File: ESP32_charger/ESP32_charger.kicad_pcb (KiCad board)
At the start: 2 copper layers, 58.2 x 36.8 mm, 60 parts, among them J1 USB_C_Receptacle_USB2.0_16P, J2 Conn_01x04_Pin, Q2 BC817W, Q3 HL-2301V, SW1 SW_Push, SW2 SW_Push, U1 ESP32-WROOM-32, U2 XM5062S, U3 HT2348ARTZ8, U4 INA219AxDCN

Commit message: update to order version
placed silkscreen
placed logos
add 3d models
generate 3d model
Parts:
- added G***: LOGO, TheBrutzlers_Lib:thebrutzler_10mm_mod, F.Cu at (96.8, 68.2)
- added REF**: OSHW-Logo2_9.8x8mm_SilkScreen, Symbol:OSHW-Logo2_9.8x8mm_SilkScreen, F.Cu at (96.2, 88.5)
- added REF**: KiCad-Logo2_6mm_SilkScreen, Symbol:KiCad-Logo2_6mm_SilkScreen, F.Cu at (84.0, 87.5)
- added SM3: SYM_Arrow45_Tiny, TheBrutzlers_Lib:Symbol_kurzschlussblog, F.Cu at (102.2, 70.9)
- SW1, SW2: footprint TheBrutzlers_Lib:microswitch -> Button_Switch_SMD:SW_SPST_CK_RS282G05A3
- moved SW2 5.34 mm to (105.5, 90.2)
- moved SW1 2.67 mm to (126.8, 90.2)
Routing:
- net Net-(U1-IO48): track 39.4 -> 45.5 mm
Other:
- board text added: "+"
- board text added: "-"
- board text added: "ESP32-charger"
- board text added: "cloneino"
- board text added: "sad_tuna"
- board text added: "v0.0001"

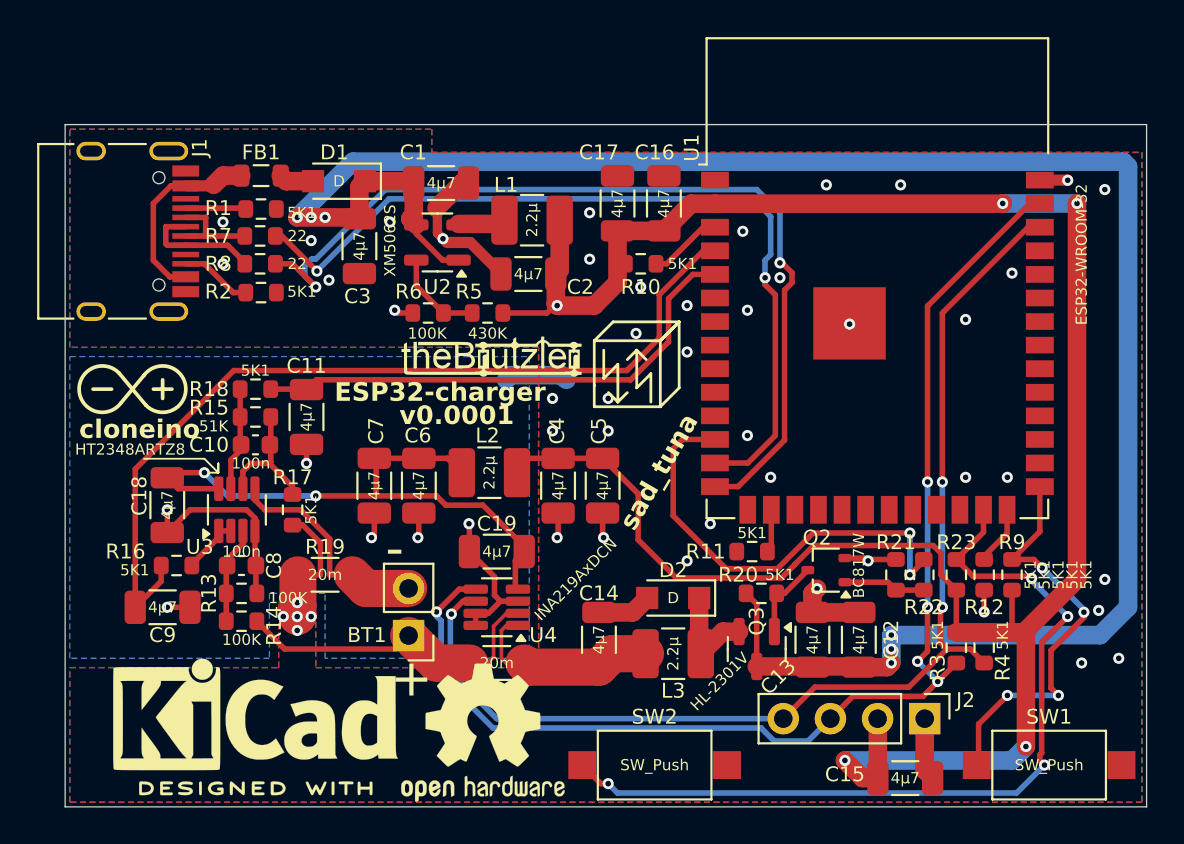
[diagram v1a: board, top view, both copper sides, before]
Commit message: add mounting holes and tuna logo
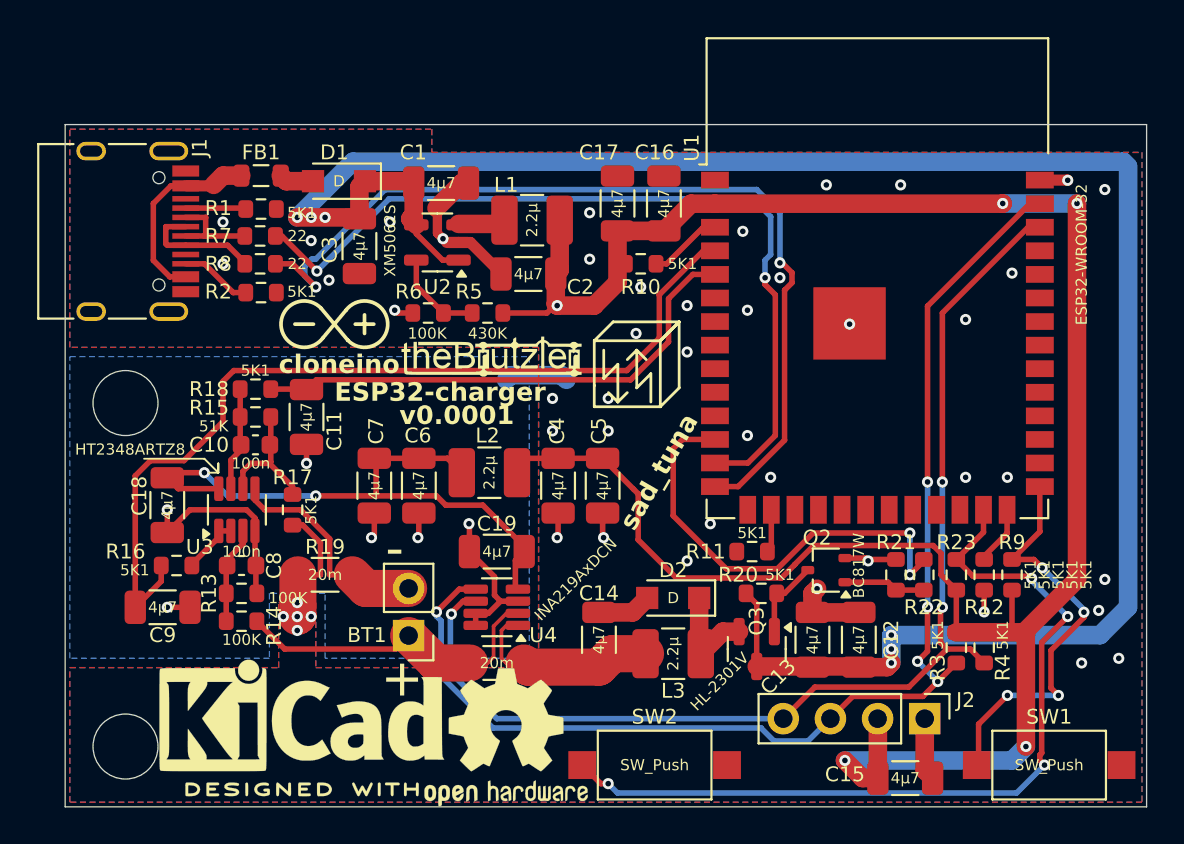
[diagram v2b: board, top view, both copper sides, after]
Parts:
- added G***: LOGO, LOGO, B.Cu at (113.0, 71.8)
- moved REF** 2.49 mm to (86.5, 87.6)
- moved REF** 1.27 mm to (97.5, 88.8)
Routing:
- net /V_BAT_ADC: track 47.7 -> 48.8 mm
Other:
- outline, holes or cut-outs redrawn
